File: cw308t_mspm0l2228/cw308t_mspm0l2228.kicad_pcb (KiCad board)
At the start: 2 copper layers, 52.3 x 68.1 mm, 29 parts, among them J11 CW308_EAST_C, J7 CW308_WEST_A, J9 CW308_SOUTH_B, SW1 RESET, U1 MSPM0L2228SPN

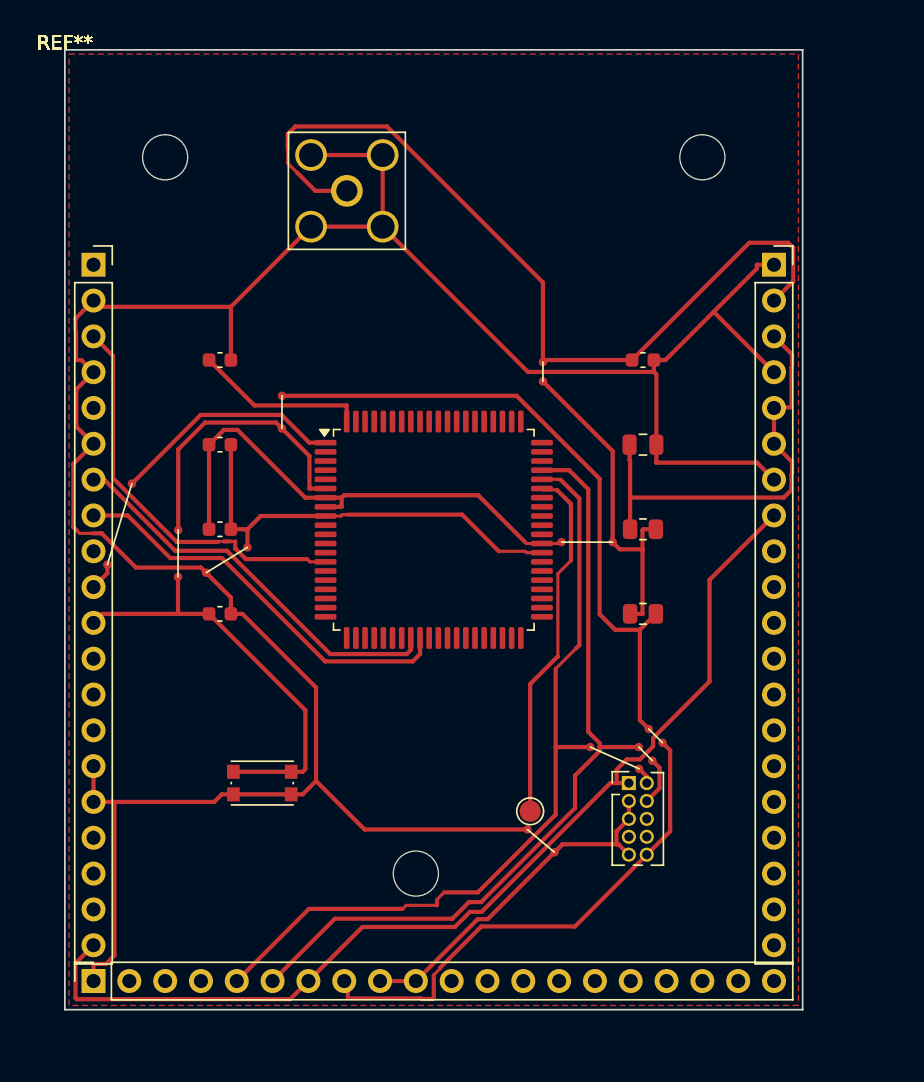
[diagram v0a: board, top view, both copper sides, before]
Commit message: PCB: CNC-ready revision (pin-through vias, 8-pin debug header, label)
- 1.0mm drilled pin-through vias (1.4mm pad), no vias under U1
- 8-pin 2.54mm debug header: 3V3, GND, SWDIO, SWCLK, TXD, RXD, RST, BSL
- Wider traces (0.4mm power / 0.3mm signal), 0.8mm pour isolation
- "WolfSniff - Group 741" copper label
- CNC export (cnc/ + cw308t_mspm0l2228_cnc.zip), regenerated gerbers

Co-Authored-By: Claude Opus 5.5 <noreply@anthropic.com>
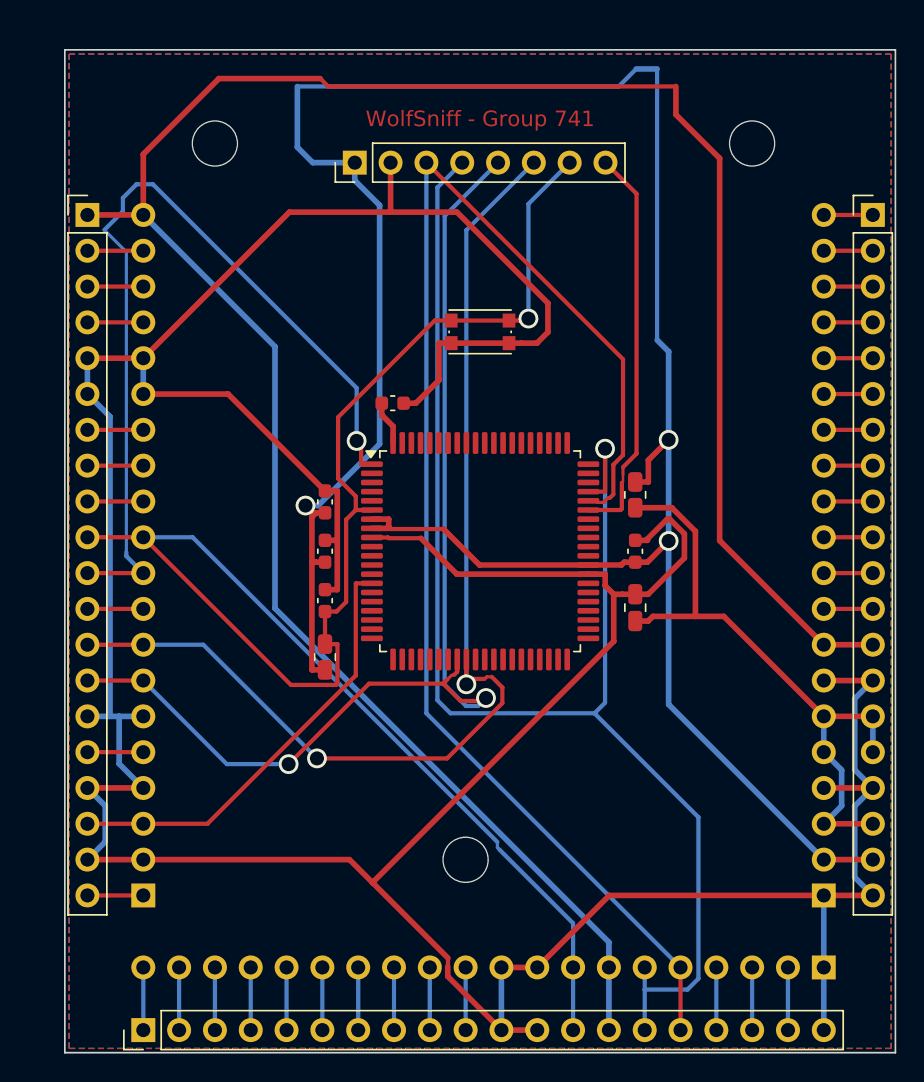
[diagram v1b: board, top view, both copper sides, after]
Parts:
- removed H1, H2, H3: MountingHole_M3, MountingHole_3.2mm_M3
- removed J11: CW308_EAST_C, PinSocket_1x20_P2.54mm_Vertical
- removed J7: CW308_WEST_A, PinSocket_1x20_P2.54mm_Vertical
- removed J9: CW308_SOUTH_B, PinSocket_1x20_P2.54mm_Vertical
- removed JP1: link 3.44mm, sca:JUMP
- removed JP10, JP3: link 1.37mm, sca:JUMP
- removed JP2: link 2.51mm, sca:JUMP
- removed JP4: link 3.63mm, sca:JUMP
- removed JP5: link 1.38mm, sca:JUMP
- removed JP6: link 3.33mm, sca:JUMP
- removed JP7: link 2.32mm, sca:JUMP
- removed JP8: link 6.01mm, sca:JUMP
- removed JP9: link 3.79mm, sca:JUMP
- removed J_MEAS: MEAS_SMA, SMA_Amphenol_132203-12_Horizontal
- removed J_SWD: CORTEX_SWD, PinHeader_2x05_P1.27mm_Vertical
- removed TP_BSL: BSL(PA18), TestPoint_Pad_D1.5mm
- added HOLE1: M3, MountingHole_3.2mm_M3, F.Cu at (28.4, 57.4)
- added HOLE2: M3, MountingHole_3.2mm_M3, F.Cu at (10.6, 6.64)
- added HOLE3: M3, MountingHole_3.2mm_M3, F.Cu at (48.7, 6.64)
- added J1: CW308_WEST_A, PinSocket_1x20_P2.54mm_Vertical, B.Cu at (5.56, 60.0)
- added J3: CW308_EAST_C, PinSocket_1x20_P2.54mm_Vertical, B.Cu at (53.8, 60.0)
- added J4: CW308_SOUTH_B, PinSocket_1x20_P2.54mm_Vertical, B.Cu at (53.8, 65.1)
- added J_DBG: DEBUG, PinHeader_1x08_P2.54mm_Vertical, F.Cu at (20.6, 8.00)
- added P1: WEST_BRK, PinHeader_1x20_P2.54mm_Vertical, F.Cu at (1.60, 11.7)
- added P3: EAST_BRK, PinHeader_1x20_P2.54mm_Vertical, F.Cu at (57.3, 11.7)
- added P4: SOUTH_BRK, PinHeader_1x20_P2.54mm_Vertical, F.Cu at (5.56, 69.5)
- R1: value R_SHUNT_DNP -> 0R_shunt_DNP
- moved SW1 35.5 mm to (29.5, 20.0)
- moved R2 22.8 mm to (18.5, 43.1), turned to 90 degrees
- moved C3 13.6 mm to (40.5, 35.6), turned to 90 degrees
- moved C1 12.6 mm to (23.3, 25.1)
- moved C4 11.6 mm to (40.5, 39.6), turned to 90 degrees
- moved C2 10.6 mm to (18.5, 35.6), turned to 90 degrees
- moved C5 7.70 mm to (18.5, 32.1), turned to 90 degrees
- moved C6 7.51 mm to (18.5, 39.1), turned to 90 degrees
- moved U1 3.62 mm to (29.5, 35.6)
- moved R1 2.50 mm to (40.5, 31.6), turned to 90 degrees
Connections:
- C2 pad 2: GND~1 -> GND
- C3 pad 1: VDD_CHIP~1 -> VDD_CHIP
- C5 pad 2: GND~1 -> GND
- R1 pad 2: VDD_CHIP~2 -> VDD_CHIP
- R2 pad 1: VDD_CHIP~2 -> VDD_CHIP
- R2 pad 2: nRST~1 -> nRST
- U1 pad 48: GND~1 -> GND
- U1 pad 6: nRST~3 -> nRST
- U1 pad 9: GND~1 -> GND
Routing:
- net VDD_CHIP: track 36.7 -> 171.0 mm, vias 0 -> 3
- net GND: track 191.6 -> 296.5 mm
- net VREF_SUPPLY: track 74.1 -> 167.4 mm
- net nRST: track 30.1 -> 123.2 mm, vias 0 -> 1
- net VDD_CHIP~1: track 61.3 -> 0.00 mm
- net UART_RX: track 28.8 -> 79.2 mm, vias 0 -> 2
- net UART_TX: track 28.6 -> 78.3 mm, vias 0 -> 2
- net SWCLK: track 56.8 -> 104.1 mm, vias 0 -> 1
- net nRST~1: track 46.8 -> 0.00 mm
- net TRIG: track 16.6 -> 61.5 mm, vias 0 -> 1
- net SWDIO: track 56.5 -> 100.6 mm
- net nRST~2: track 36.6 -> 0.00 mm
- net GND~1: track 30.9 -> 0.00 mm
- net GND~2: track 25.4 -> 0.00 mm
- net VDD_CHIP~2: track 23.6 -> 0.00 mm
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- added copper zone on B.Cu, net GND
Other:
- board size 52.3 x 68.1 mm -> 58.9 x 71.1 mm
- board text added: "WolfSniff - Group 741"

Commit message: PCB: correct MSPM0L2228 package, no traces under the chip
- U1 footprint LQFP-80_14x14mm_P0.65mm -> LQFP-80_12x12mm_P0.5mm
  (TI PN0080A: 12x12 body, 14x14 over leads, 0.5mm pitch)
- Routing keepout under the chip body on both layers (VDD/GND crossed it)
- Re-routed: 0 unconnected, 0 clearance; 10 vias, none under U1
- Power 0.4mm, necked to 0.3mm at the 0.25mm QFP pads
- Regenerated CNC files, gerbers, renders; BOM/README/schematic updated

Co-Authored-By: Claude Opus 5.5 <noreply@anthropic.com>
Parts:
- U1: footprint LQFP-80_14x14mm_P0.65mm -> LQFP-80_12x12mm_P0.5mm
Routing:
- net GND: track 296.5 -> 400.8 mm, vias 0 -> 1
- net VREF_SUPPLY: track 167.4 -> 130.2 mm
- net SWDIO: track 100.6 -> 129.5 mm, vias 0 -> 1
- net SWCLK: track 104.1 -> 76.2 mm, vias 1 -> 2
- net nRST: track 123.2 -> 142.5 mm
- net VCORE: track 3.19 -> 18.3 mm, vias 0 -> 2
- net TRIG: track 61.5 -> 74.5 mm
- net VDD_CHIP: track 171.0 -> 164.5 mm, vias 3 -> 0
- net UART_TX: track 78.3 -> 82.2 mm, vias 2 -> 1
- net FILT_OUT: track 45.6 -> 43.5 mm
- net CLKIN: track 31.1 -> 32.6 mm, vias 0 -> 1
- net UART_RX: track 79.2 -> 80.1 mm, vias 2 -> 0
